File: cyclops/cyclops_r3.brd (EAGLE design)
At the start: 124.5 x 79.9 mm, 138 parts, among them Q1 BC817, Q2 IRF510, U1 MCP4921, U10 TLV2374, U11 THS4281, U12 MAX4564, U13 ZXTD, U14 ZXTD, U2 ADG3301, U3 MCP4022-50k, U4 LT1931, U5 LT1764A, U6 337L, U7 TLV3701, U8 ADR03, U9 OP1177, X1 SLP3, X2 SLP3, X3 SLP3

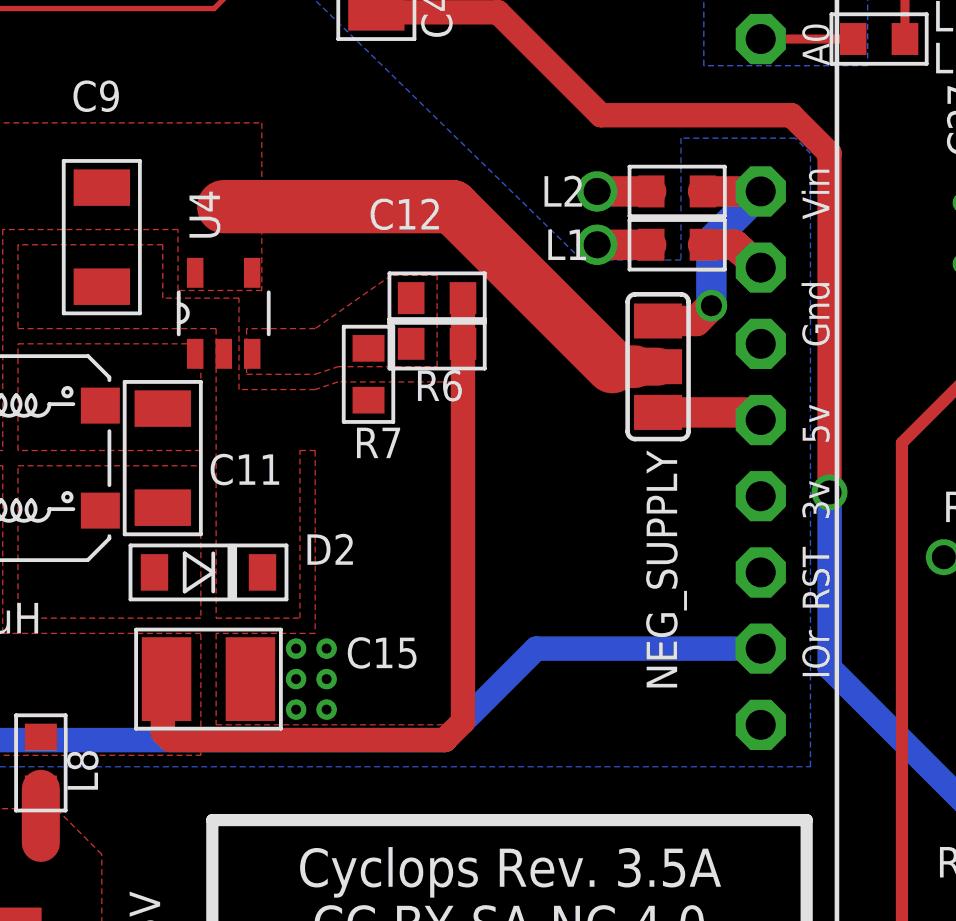
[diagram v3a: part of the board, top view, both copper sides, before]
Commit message: Got rid of negative supply source jumper.
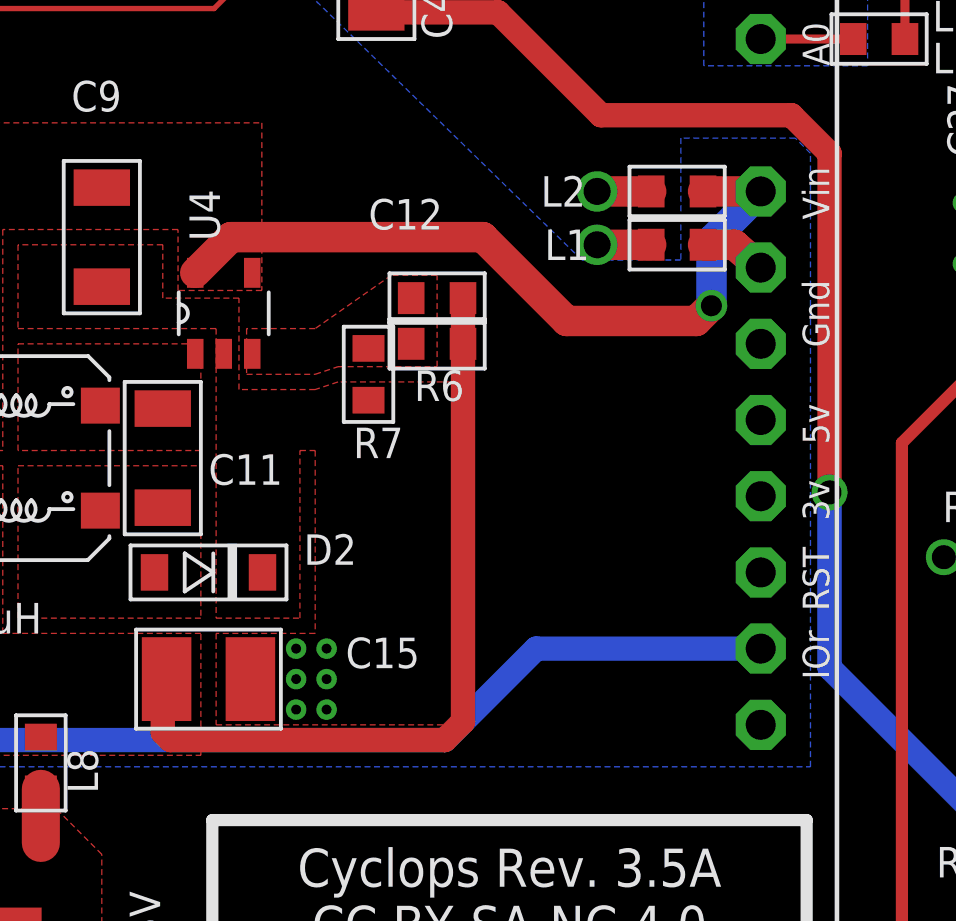
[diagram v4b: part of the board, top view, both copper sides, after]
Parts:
- removed NEG_SUPPLY: (no value), cyclops:SJ_2
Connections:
- removed net VIN: C9.1, L7.3, NEG_SUPPLY.2, U4.4, U4.5
- net +5V: no longer NEG_SUPPLY.1
- net VIN_ARDUINO: now also C9.1, L7.3, U4.4, U4.5; no longer NEG_SUPPLY.3
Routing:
- net VIN_ARDUINO: track 8.40 -> 25.5 mm
- net VIN: track 16.7 -> 0.00 mm
- net +5V: track 19.1 -> 15.6 mm
- added copper zone on layer 1, net VIN_ARDUINO
- removed copper zone on layer 1, net VIN
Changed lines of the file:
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@@
 <attribute name="VALUE" x="81.661" y="40.894" size="1.016" layer="27" font="vector" ratio="18" align="center-left"/>
-</element>
-<element name="NEG_SUPPLY" library="cyclops" package="SJ_2" value="" x="52.07" y="39.878" smashed="yes" rot="R90">
-<attribute name="NAME" x="51.689" y="37.084" size="1.016" layer="25" font="vector" ratio="18" rot="R270"/>
-<attribute name="VALUE" x="52.07" y="39.7779" size="0.02" layer="27" rot="R90"/>
 </element>
 <element name="C9" library="cyclops" package="1206" value="4.7uF" x="33.528" y="44.196" smashed="yes" rot="R270">
@@
 <wire x1="15.8496" y1="28.194" x2="15.875" y2="28.1686" width="0.4064" layer="1"/>
 <contactref element="LEONARDO" pad="5VB"/>
-<contactref element="NEG_SUPPLY" pad="1"/>
-<wire x1="52.07" y1="38.354" x2="55.238" y2="38.354" width="1.016" layer="1"/>
-<wire x1="55.238" y1="38.354" x2="55.492" y2="38.1" width="1.016" layer="1"/>
 </signal>
 <signal name="SCLK">
@@
 <contactref element="LEONARDO" pad="VIN"/>
 <wire x1="55.492" y1="45.72" x2="53.5686" y2="45.72" width="1.016" layer="1"/>
-<contactref element="NEG_SUPPLY" pad="3"/>
-<wire x1="52.07" y1="41.402" x2="53.34" y2="41.402" width="1.016" layer="1"/>
 <wire x1="53.34" y1="41.402" x2="53.848" y2="41.91" width="1.016" layer="1"/>
 <via x="53.848" y="41.91" extent="1-16" drill="0.7"/>
 <wire x1="53.848" y1="41.91" x2="53.848" y2="44.076" width="1.016" layer="16"/>
 <wire x1="53.848" y1="44.076" x2="55.492" y2="45.72" width="1.016" layer="16"/>
+<contactref element="U4" pad="5"/>
+<contactref element="U4" pad="4"/>
+<polygon width="0.127" layer="1" thermals="no">
+<vertex x="30.226" y="37.084"/>
+<vertex x="26.416" y="37.084"/>
+<vertex x="26.416" y="48.006"/>
+<vertex x="38.862" y="48.006"/>
+<vertex x="38.862" y="42.418"/>
+<vertex x="36.068" y="42.418"/>
+<vertex x="36.068" y="44.45"/>
+<vertex x="30.226" y="44.45"/>
+</polygon>
+<contactref element="L7" pad="3"/>
+<contactref element="C9" pad="1"/>
+<wire x1="53.34" y1="41.402" x2="49.022" y2="41.402" width="1.016" layer="1"/>
+<wire x1="49.022" y1="41.402" x2="46.228" y2="44.196" width="1.016" layer="1"/>
+<wire x1="46.228" y1="44.196" x2="37.832" y2="44.196" width="1.016" layer="1"/>
+<wire x1="37.832" y1="44.196" x2="36.642" y2="43.006" width="1.016" layer="1"/>
 </signal>
 <signal name="N$29">
@@
 </polygon>
 </signal>
-<signal name="VIN">
-<contactref element="U4" pad="5"/>
-<contactref element="U4" pad="4"/>
-<polygon width="0.127" layer="1" thermals="no">
-<vertex x="30.226" y="37.084"/>
-<vertex x="26.416" y="37.084"/>
-<vertex x="26.416" y="48.006"/>
-<vertex x="38.862" y="48.006"/>
-<vertex x="38.862" y="42.418"/>
-<vertex x="36.068" y="42.418"/>
-<vertex x="36.068" y="44.45"/>
-<vertex x="30.226" y="44.45"/>
-</polygon>
-<contactref element="L7" pad="3"/>
-<contactref element="NEG_SUPPLY" pad="2"/>
-<wire x1="52.07" y1="39.878" x2="51.308" y2="39.878" width="1.27" layer="1"/>
-<wire x1="51.308" y1="39.878" x2="50.546" y2="39.878" width="1.4224" layer="1"/>
-<wire x1="50.546" y1="39.878" x2="45.212" y2="45.212" width="1.778" layer="1"/>
-<wire x1="45.212" y1="45.212" x2="37.592" y2="45.212" width="1.778" layer="1"/>
-<contactref element="C9" pad="1"/>
-</signal>
 <signal name="COM">

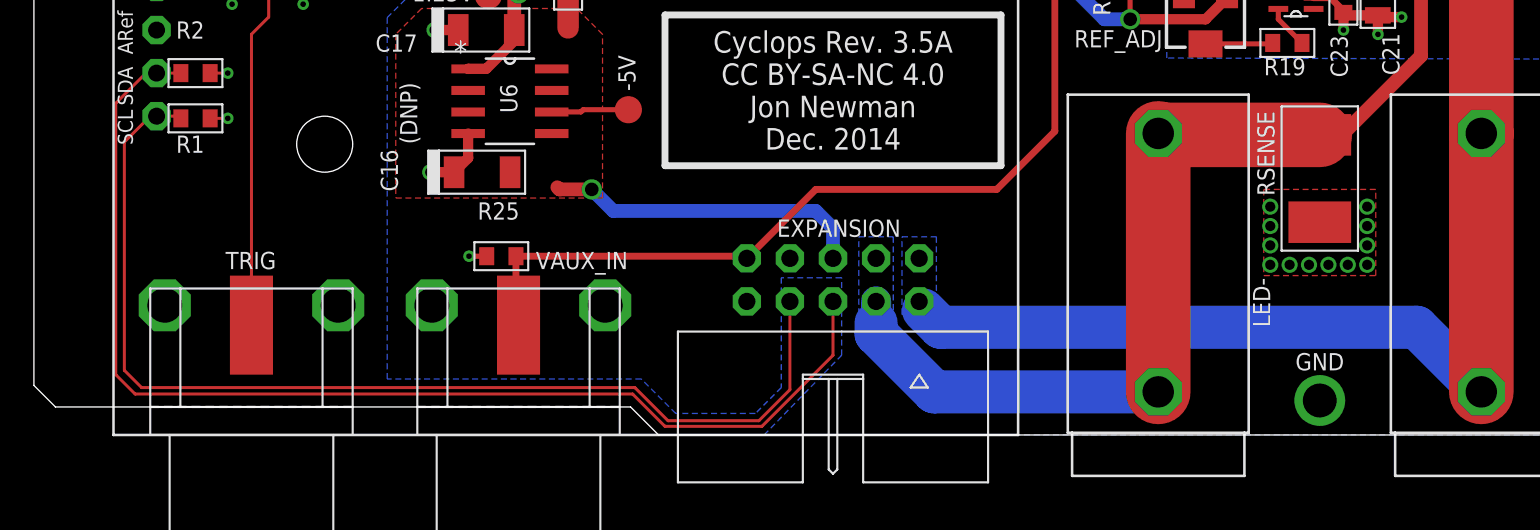
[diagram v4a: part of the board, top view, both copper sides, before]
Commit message: Taking care of some of the TODOs
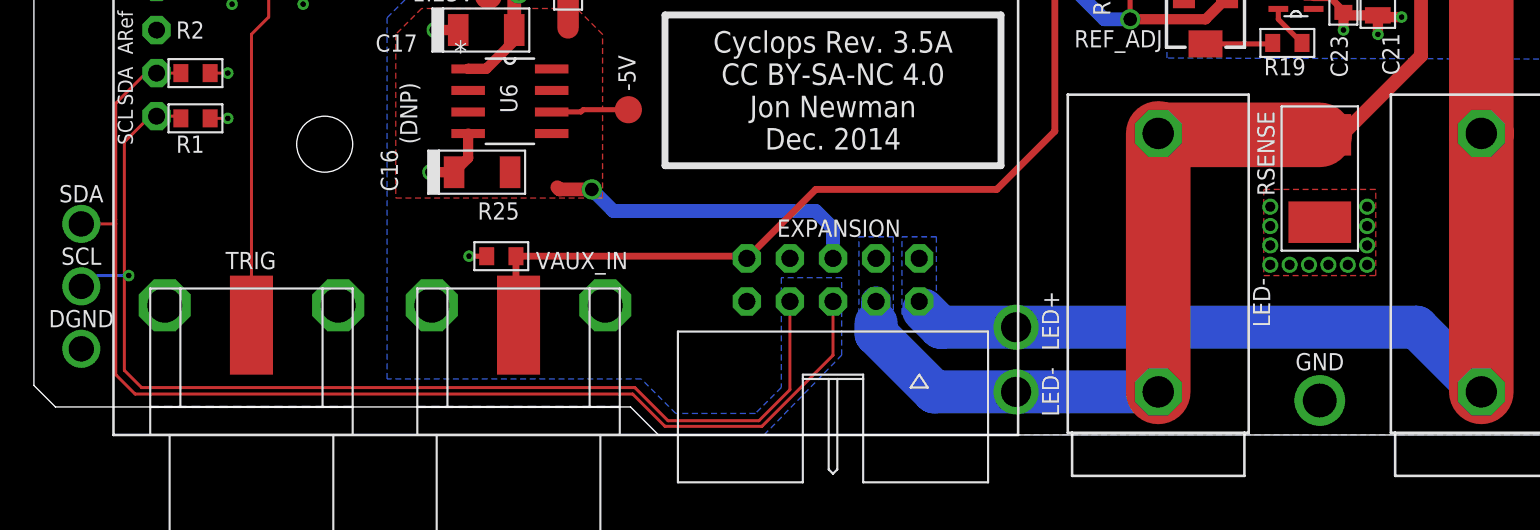
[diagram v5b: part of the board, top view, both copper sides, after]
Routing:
- net SCL: track 63.9 -> 67.2 mm, vias 0 -> 2
- net SDA: track 69.0 -> 71.1 mm, vias 0 -> 1
- net LED-: vias 0 -> 1
- net LED+: vias 0 -> 1
- net GND: vias 124 -> 125
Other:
- board text added: "DGND"
- board text added: "LED+"
- board text added: "LED-"
- board text added: "SCL"
- board text added: "SDA"
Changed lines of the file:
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@@
 <text x="42.418" y="64.262" size="1.016" layer="21" font="vector" ratio="18" rot="R90" align="center-left">FIXD</text>
 <text x="41.275" y="64.262" size="1.016" layer="21" font="vector" ratio="18" rot="R90" align="center-left">PROT</text>
+<text x="59.944" y="2.54" size="1.016" layer="21" font="vector" ratio="18" rot="R270" align="center">LED-</text>
+<text x="59.944" y="6.731" size="1.016" layer="21" font="vector" ratio="18" rot="R270" align="center">LED+</text>
+<text x="2.794" y="6.858" size="1.016" layer="21" font="vector" ratio="18" align="center">DGND</text>
+<text x="2.794" y="10.541" size="1.016" layer="21" font="vector" ratio="18" align="center">SCL</text>
+<text x="2.794" y="14.224" size="1.016" layer="21" font="vector" ratio="18" align="center">SDA</text>
 </plain>
 <attributes>
@@
 <wire x1="21.971" y1="79.248" x2="23.241" y2="77.978" width="0.3048" layer="2"/>
 <via x="117.221" y="66.802" extent="1-16" drill="2" shape="octagon" alwaysstop="yes"/>
+<via x="2.794" y="5.08" extent="1-16" drill="1.5" shape="octagon" alwaysstop="yes"/>
 <wire x1="95.504" y1="56.515" x2="100.965" y2="57.15" width="0" layer="19" extent="1-1"/>
 <wire x1="91.694" y1="57.15" x2="91.694" y2="56.515" width="0" layer="19" extent="1-1"/>
@@
 <contactref element="EXPANSION" pad="1"/>
 <wire x1="85.344" y1="2.54" x2="81.534" y2="6.35" width="2.54" layer="16"/>
-<wire x1="81.534" y1="6.35" x2="53.467" y2="6.35" width="2.54" layer="16"/>
+<wire x1="81.534" y1="6.35" x2="57.912" y2="6.35" width="2.54" layer="16"/>
 <polygon width="0.254" layer="16" thermals="no">
 <vertex x="51.181" y="11.684"/>
@@
 <vertex x="51.181" y="7.112"/>
 </polygon>
+<wire x1="57.912" y1="6.35" x2="53.467" y2="6.35" width="2.54" layer="16"/>
 <wire x1="53.467" y1="6.35" x2="52.451" y2="7.366" width="2.54" layer="16"/>
 <wire x1="52.451" y1="7.366" x2="52.451" y2="7.62" width="1.4224" layer="16"/>
 <wire x1="52.451" y1="7.62" x2="52.197" y2="7.874" width="1.4224" layer="16"/>
+<via x="57.912" y="6.35" extent="1-16" drill="1.778" shape="octagon"/>
 </signal>
 <signal name="N$2">
@@
 <contactref element="EXPANSION" pad="3"/>
 <contactref element="EXPANSION" pad="4"/>
-<wire x1="66.294" y1="2.54" x2="53.086" y2="2.54" width="2.54" layer="16"/>
+<wire x1="66.294" y1="2.54" x2="57.912" y2="2.54" width="2.54" layer="16"/>
 <polygon width="0.254" layer="16" thermals="no">
 <vertex x="48.641" y="11.684"/>
@@
 <vertex x="48.641" y="7.112"/>
 </polygon>
+<wire x1="57.912" y1="2.54" x2="53.086" y2="2.54" width="2.54" layer="16"/>
 <wire x1="85.2805" y1="36.449" x2="82.8675" y2="36.449" width="0.4064" layer="1"/>
 <wire x1="82.8675" y1="36.449" x2="82.677" y2="36.2585" width="0.4064" layer="1"/>
@@
 <wire x1="49.657" y1="5.969" x2="49.657" y2="6.604" width="2.54" layer="16"/>
 <wire x1="49.657" y1="6.604" x2="49.657" y2="7.874" width="1.778" layer="16"/>
+<via x="57.912" y="2.54" extent="1-16" drill="1.778" shape="octagon"/>
 </signal>
 <signal name="N$17">
@@
 <wire x1="7.232" y1="21.336" x2="6.604" y2="21.336" width="0.1778" layer="1"/>
 <wire x1="6.604" y1="21.336" x2="4.826" y2="19.558" width="0.1778" layer="1"/>
-<wire x1="4.826" y1="19.558" x2="4.826" y2="3.556" width="0.1778" layer="1"/>
+<wire x1="4.826" y1="19.558" x2="4.826" y2="12.7" width="0.1778" layer="1"/>
+<wire x1="4.826" y1="12.446" x2="4.826" y2="3.556" width="0.1778" layer="1"/>
 <wire x1="4.826" y1="3.556" x2="5.969" y2="2.413" width="0.1778" layer="1"/>
 <wire x1="5.969" y1="2.413" x2="35.306" y2="2.413" width="0.1778" layer="1"/>
@@
 <contactref element="R2" pad="2"/>
 <wire x1="8.6614" y1="21.336" x2="7.232" y2="21.336" width="0.1778" layer="1"/>
+<via x="2.794" y="12.446" extent="1-16" drill="1.5" shape="octagon"/>
+<wire x1="2.794" y1="12.446" x2="4.826" y2="12.446" width="0.1778" layer="1"/>
+<wire x1="4.826" y1="12.446" x2="4.826" y2="12.7" width="0.1778" layer="1"/>
 </signal>
 <signal name="SCL">
 <contactref element="LEONARDO" pad="SCL"/>
-<wire x1="5.334" y1="17.272" x2="5.334" y2="3.81" width="0.1778" layer="1"/>
 <wire x1="5.334" y1="3.81" x2="6.35" y2="2.794" width="0.1778" layer="1"/>
 <wire x1="6.35" y1="2.794" x2="35.433" y2="2.794" width="0.1778" layer="1"/>
@@
 <wire x1="8.6614" y1="18.669" x2="8.5344" y2="18.796" width="0.1778" layer="1"/>
 <wire x1="8.5344" y1="18.796" x2="7.232" y2="18.796" width="0.1778" layer="1"/>
+<via x="2.794" y="8.763" extent="1-16" drill="1.5" shape="octagon"/>
+<via x="5.588" y="9.398" extent="1-16" drill="0.3302"/>
+<wire x1="5.334" y1="17.272" x2="5.334" y2="9.398" width="0.1778" layer="1"/>
+<wire x1="5.588" y1="9.398" x2="5.334" y2="9.398" width="0.1778" layer="1"/>
+<wire x1="5.334" y1="9.398" x2="5.334" y2="3.81" width="0.1778" layer="1"/>
+<wire x1="5.588" y1="9.398" x2="3.429" y2="9.398" width="0.1778" layer="16"/>
+<wire x1="3.429" y1="9.398" x2="2.794" y2="8.763" width="0.1778" layer="16"/>
 </signal>
 <signal name="N$11">
